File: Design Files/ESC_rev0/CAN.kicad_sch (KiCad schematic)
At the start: 11 parts, among them J7 Conn_01x04, U6 ESDCAN24-2BLY, U7 SN65HVD230

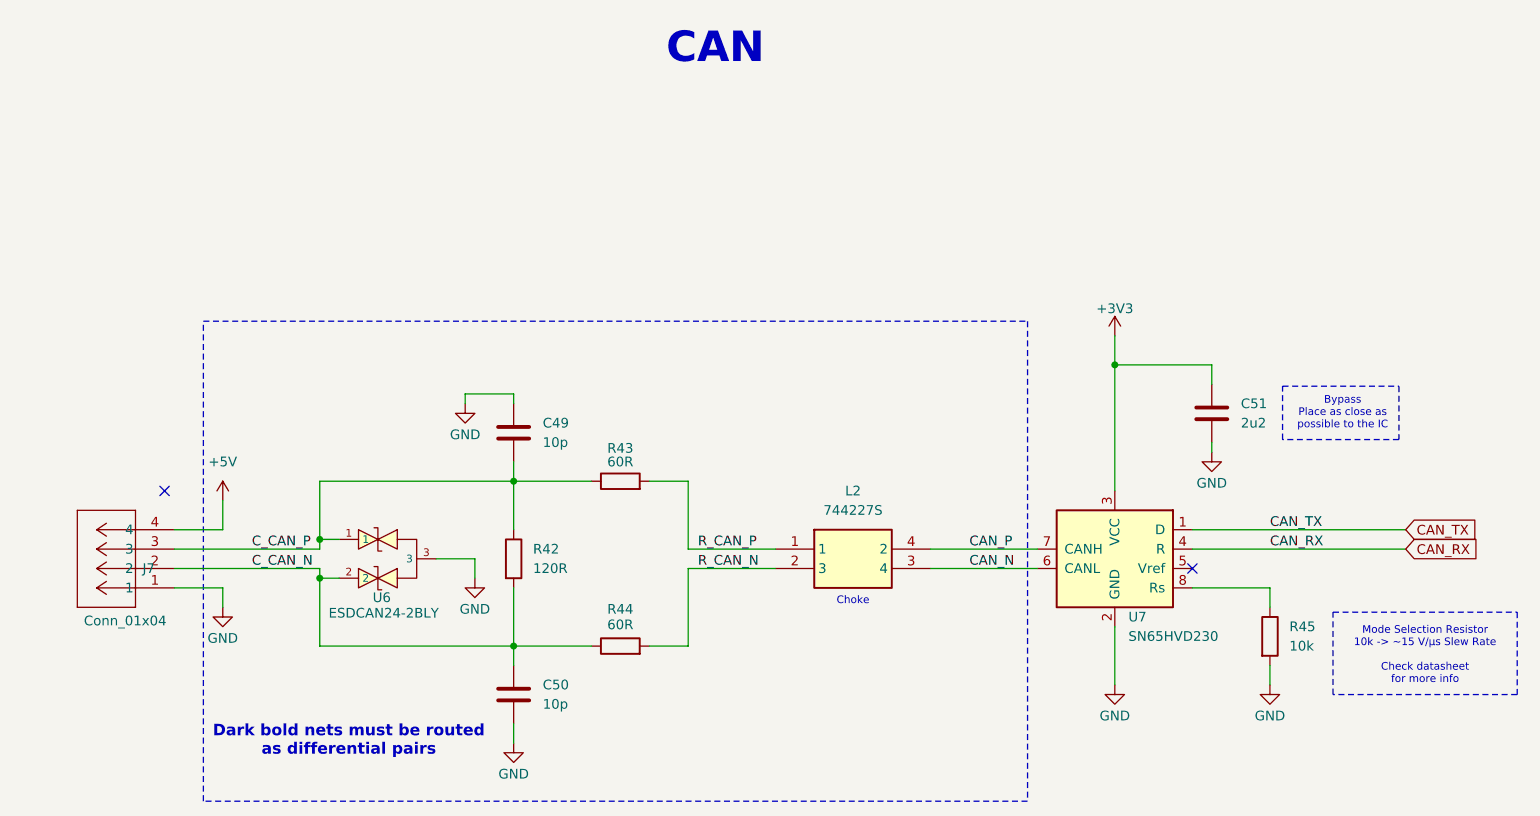
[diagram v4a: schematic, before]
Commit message: update 16
All components placed on board. Some components modifications and addition were made: added 3D models, changed some symbols and footprints positions and some component types.
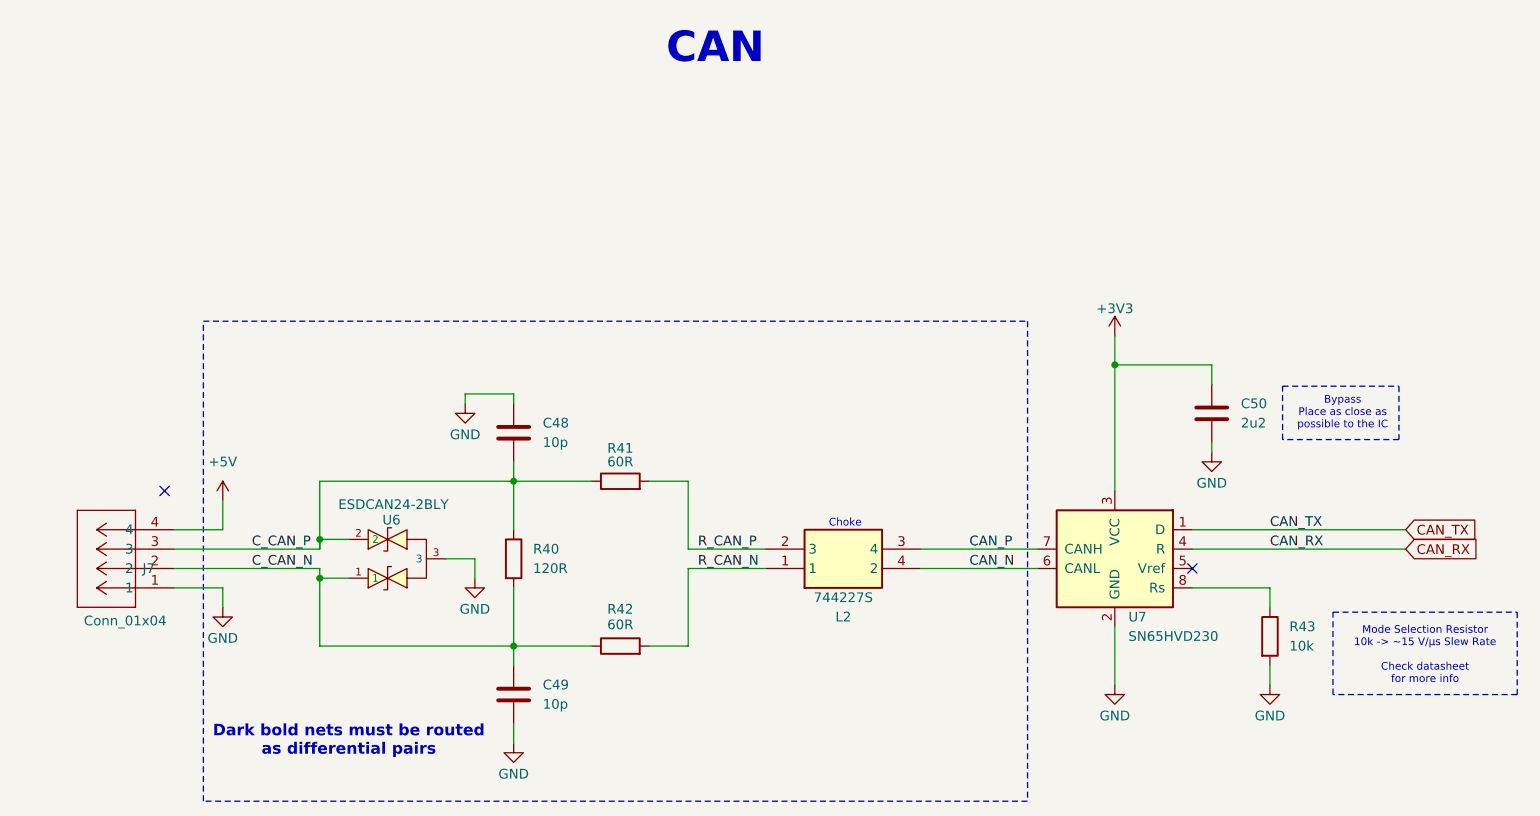
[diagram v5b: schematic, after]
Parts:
- C48: renamed from C49; footprint Capacitor_SMD:C_0201_0603Metric -> Capacitor_SMD:C_0603_1608Metric
- C49: renamed from C50; footprint Capacitor_SMD:C_0201_0603Metric -> Capacitor_SMD:C_0603_1608Metric
- C50: renamed from C51; footprint Capacitor_SMD:C_0201_0603Metric -> Capacitor_SMD:C_0603_1608Metric
- L2: footprint WE-SL274 -> 744227S_foot:WE-SL274
- renumbered R42 to R40, R43 to R41, R44 to R42, R45 to R43
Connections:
- net CAN_N: now also L2.4 (2); no longer L2.3 (4)
- net CAN_P: now also L2.3 (4); no longer L2.4 (2)
- net C_CAN_N: now also U6.1; no longer U6.2
- net C_CAN_P: now also U6.2; no longer U6.1
- net R_CAN_N: now also L2.1; no longer L2.2 (3)
- net R_CAN_P: now also L2.2 (3); no longer L2.1
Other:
- moved on the sheet: U6
